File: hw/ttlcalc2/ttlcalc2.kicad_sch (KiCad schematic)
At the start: 52 parts, among them J1 POWER, J2 RST, J3 IO_BUS, J4 EXT_CLK, J5 CLK_SRC, U1 74LS163, U10 74LS273, U11 74LS273, U12 74LS283, U13 74LS08, U14 74LS138, U15 74LS138, U16 74LS04, U17 74LS08, U18 74LS151, U19 74LS191, U2 74LS163, U20 74LS191, U21 74LS157, U22 74LS08, U23 74LS373, U24 74LS244, U25 74LS173, U26 2101, U27 74LS157, U28 74LS173, U29 74LS244, U3 74LS163, U30 74LS244, U31 74LS244, U32 74LS73, U33 74LS00, U34 74LS73, U35 74LS173, U4 74LS173, U5 74LS173, U6 27C64, U7 27C64, U8 74LS181, U9 74LS283, X1 TCXO3

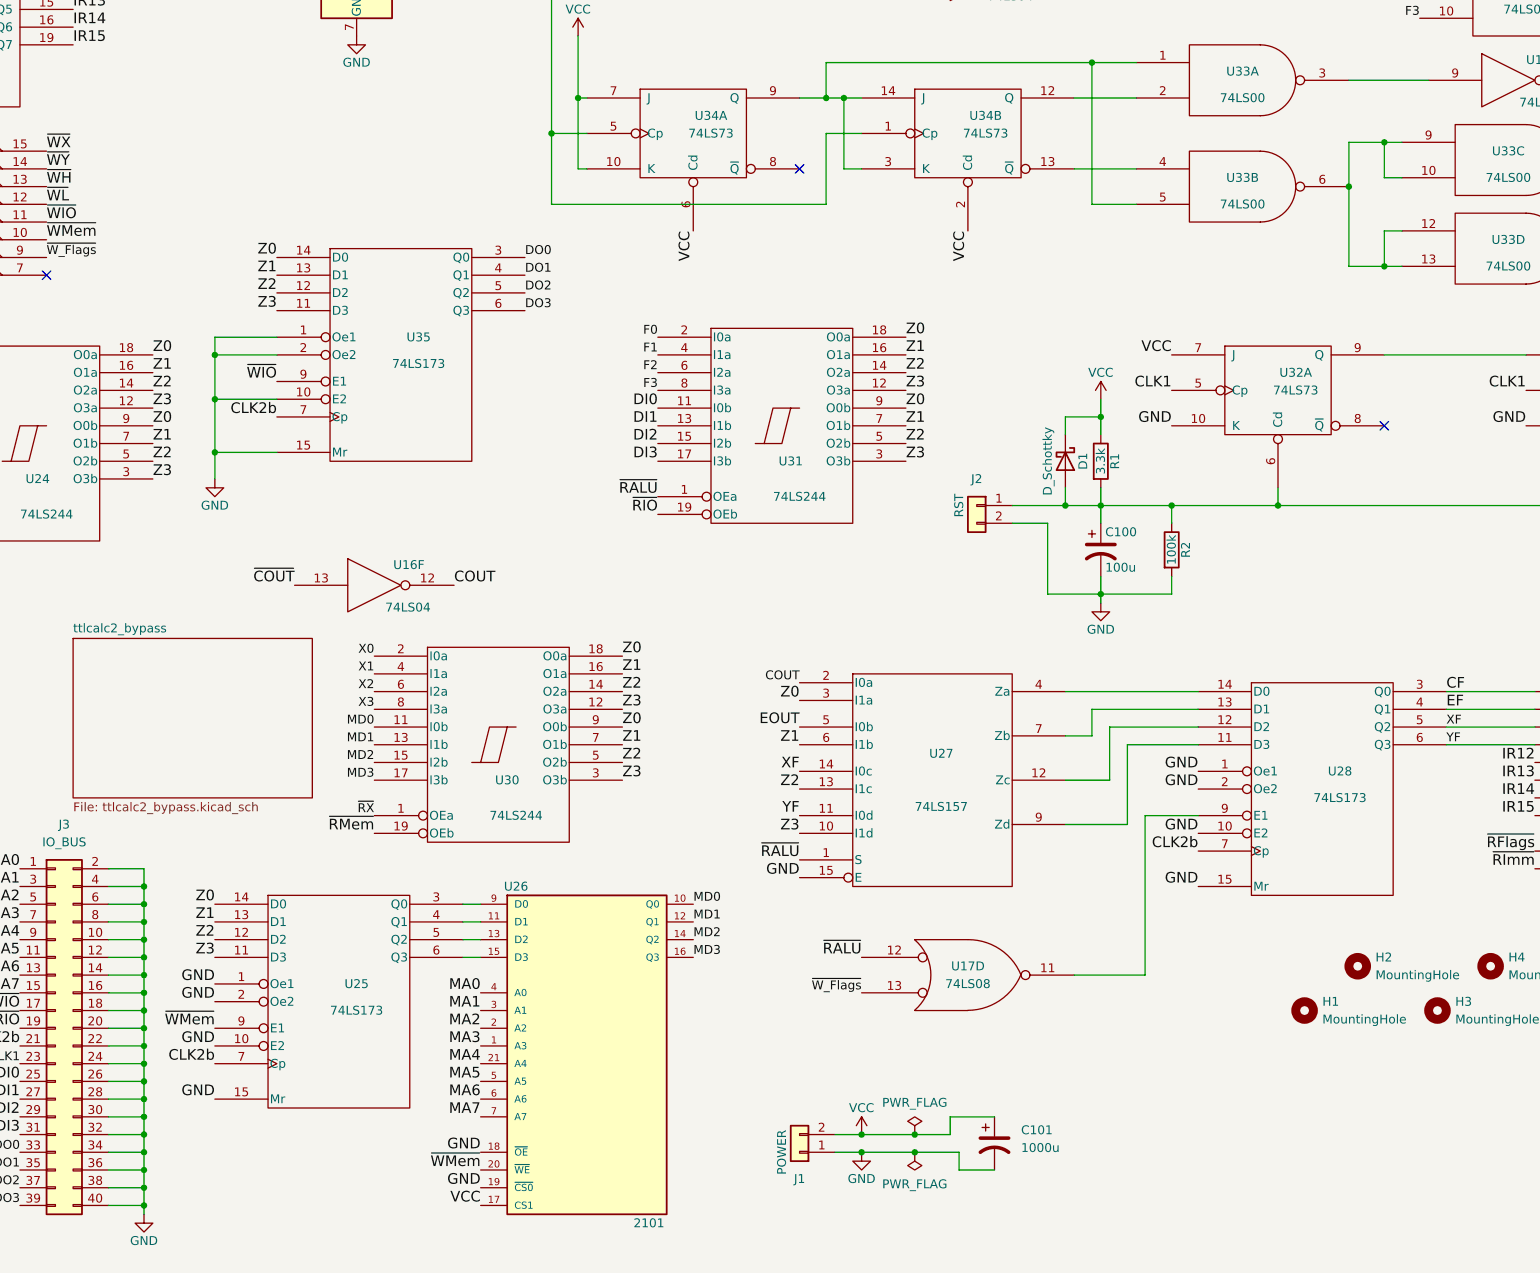
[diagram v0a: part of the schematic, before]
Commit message: Memory and I/O timing improvements
Changed memory /WE to use combination of /CLK2 and /WMem to ensure /WE is de-asserted well before memory address becomes invalid
Removed memory data input register, made unnecessary by above change
Changed I/O output register to buffer (same reasons above)
Fixed and updated date on PCB silkscreen
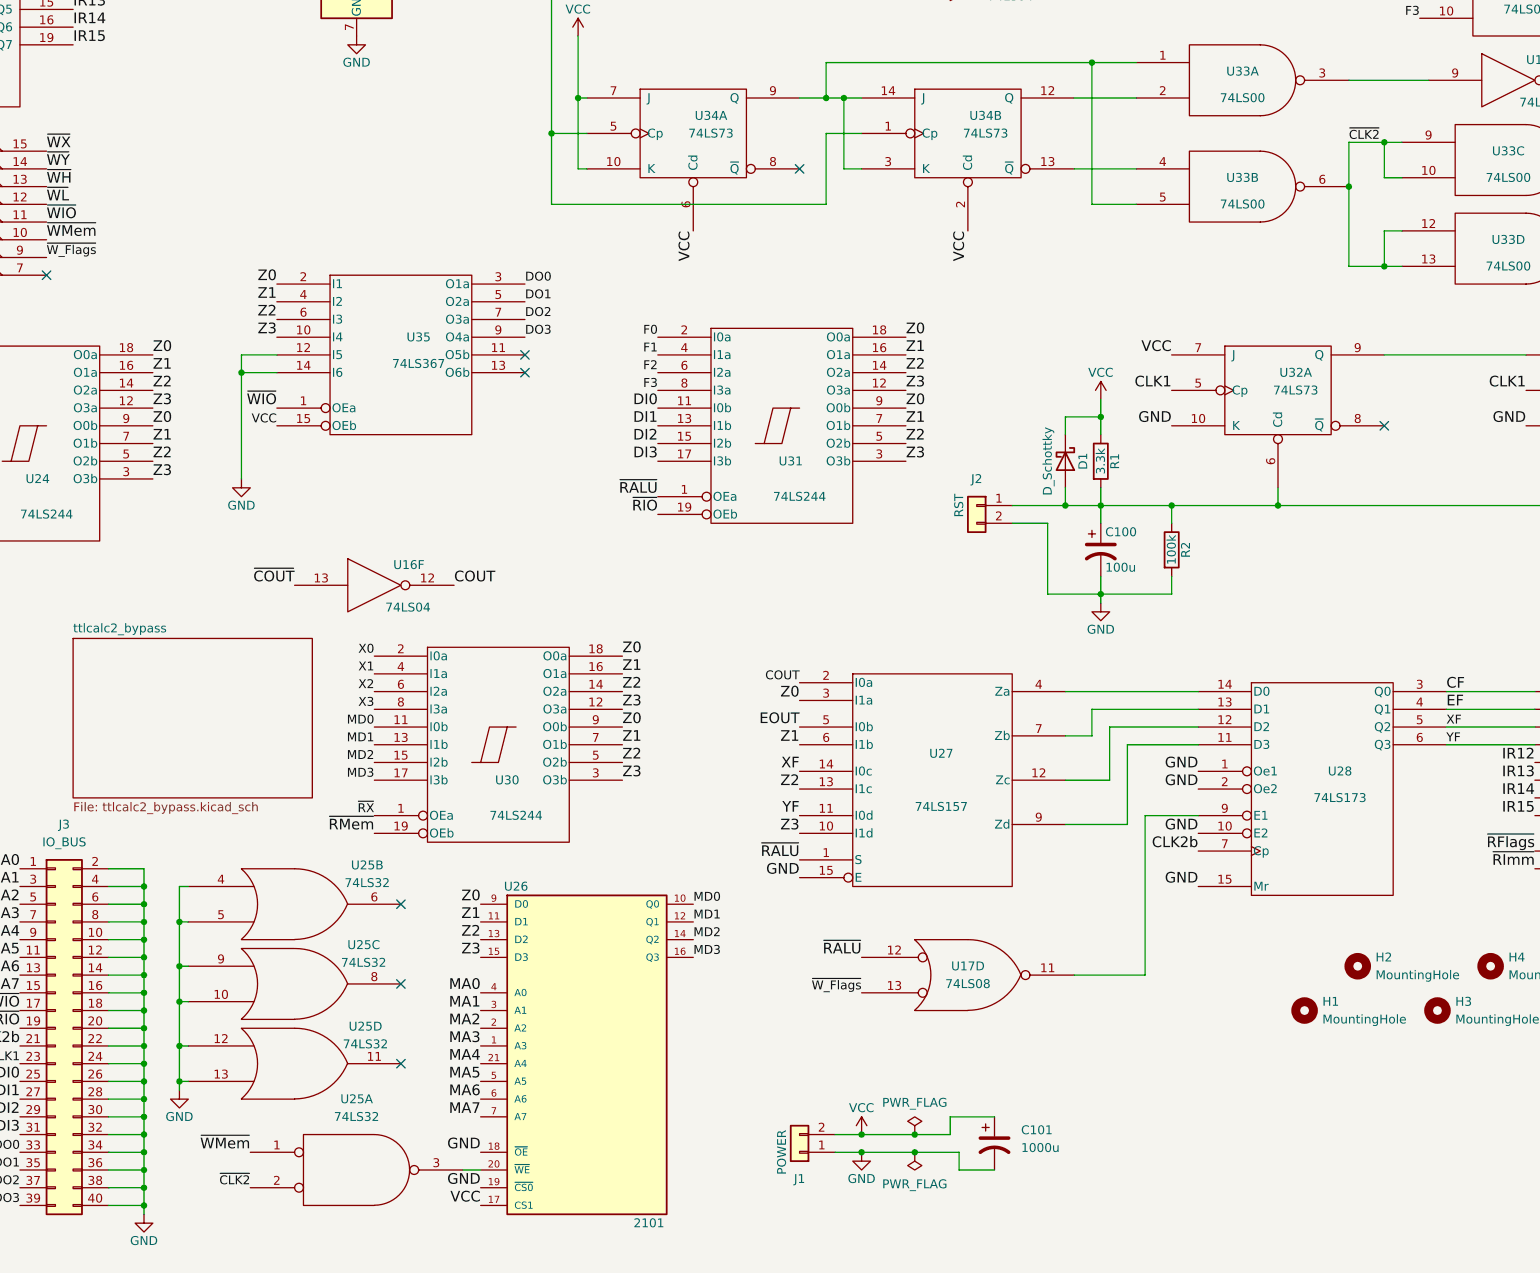
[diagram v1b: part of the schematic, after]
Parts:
- removed U25: 74LS173, Package_DIP:DIP-16_W7.62mm, symbol 74xx1:74LS173
- added U25: 74LS32, Package_DIP:DIP-14_W7.62mm, symbol 74xx1:74LS32
- U35: value 74LS173 -> 74LS367; symbol 74xx1:74LS173 -> 74xx1:74LS367
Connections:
- net CLK2b: no longer U35.7 (Cp)
- net DO1: now also U35.5 (O2a); no longer U35.4 (Q1)
- net DO2: now also U35.7 (O3a); no longer U35.5 (Q2)
- net DO3: now also U35.9 (O4a); no longer U35.6 (Q3)
- net GND: now also U35.12 (I5), U35.14 (I6), U25.10, U25.12, U25.13, U25.4, U25.5, U25.7 (GND), U25.7 (GND), U25.7 (GND), U25.7 (GND), U25.9; no longer U35.1 (Oe1), U35.10 (E2), U35.15 (Mr), U35.2 (Oe2)
- net VCC: now also U35.15 (OEb), U25.14 (VCC), U25.14 (VCC), U25.14 (VCC), U25.14 (VCC)
- net Z0: now also U26.9 (D0), U35.2 (I1); no longer U35.14 (D0)
- net Z1: now also U26.11 (D1), U35.4 (I2); no longer U35.13 (D1)
- net Z2: now also U26.13 (D2), U35.6 (I3); no longer U35.12 (D2)
- net Z3: now also U26.15 (D3), U35.10 (I4); no longer U35.11 (D3)
- net ~{WIO}: now also U35.1 (OEa); no longer U35.9 (E1)
- net ~{WMem}: now also U25.1; no longer U26.20 (~{WE})
- net ~{CLK2}: now reaches U33.10, U33.12, U33.13, U33.6, U33.9
- net ~{CLK2}: now also U25.2
- new net: U25.3, U26.20 (~{WE})
- no-connect marks 21 -> 26
